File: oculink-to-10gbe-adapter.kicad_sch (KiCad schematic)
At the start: 9 parts

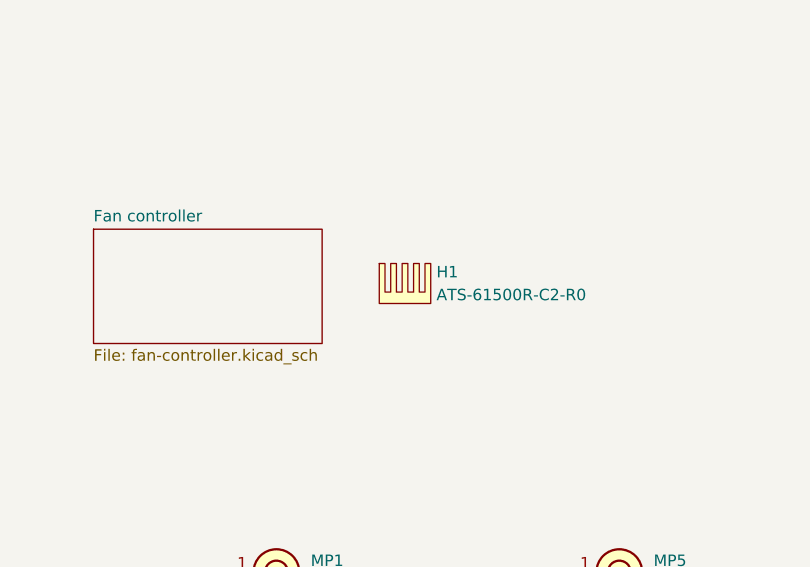
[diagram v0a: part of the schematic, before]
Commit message: Set heatsink and fan controller section as DNP
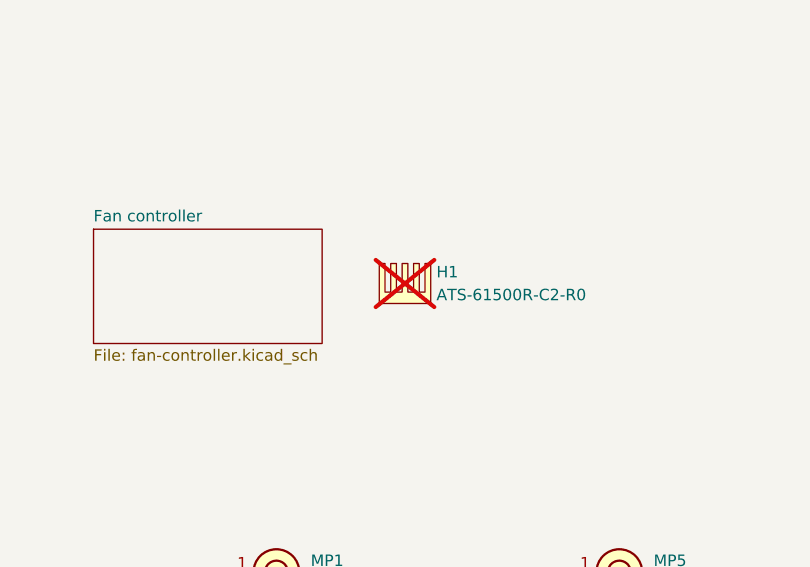
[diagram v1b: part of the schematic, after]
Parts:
- H1: now not fitted; now left out of the parts list
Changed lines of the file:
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@@
 		(unit 1)
 		(exclude_from_sim no)
-		(in_bom yes)
-		(on_board yes)
-		(dnp no)
+		(in_bom no)
+		(on_board yes)
+		(dnp yes)
 		(fields_autoplaced yes)
 		(property "Reference" "H1"
@@
 		(size 25.4 12.7)
 		(exclude_from_sim no)
-		(in_bom yes)
-		(on_board yes)
-		(dnp no)
+		(in_bom no)
+		(on_board yes)
+		(dnp yes)
 		(fields_autoplaced yes)
 		(stroke
